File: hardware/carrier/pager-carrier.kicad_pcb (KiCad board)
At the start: 2 copper layers, 38.9 x 48.9 mm, 79 parts, among them J1 PANEL, J2 CARDKB, J3 HAPTIC, J4 EXT_LED, J5 PIEZ, J6 USB4235, J7 BATTERY, J8 FRONTLIGHT, M1 Walter, Q1 UMH3N, Q2 SI1308EDL, Q3 MMST3904, Q4 AO3401A, SW1 KMR221GLFS, SW2 JS102011SAQN, U1 CP2102N-A02-GQFN24, U2 SN74LVC2G126DCUR, U3 DRV2605LDGSR, U4 LIS2DW12TR, U5 BQ25185DLHR, U6 MAX17048G+T10, U7 TPS62840DLCR

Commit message: v0.2 boards release candidate
This has almost everything in both boards but we need
a few part swaps.
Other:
- board text added: "+LED-"
- board text added: "BATT"
- board text added: "CHAM Carrier @awongawong"
- board text added: "FR. L"
- board text added: "HAPTIC"
- board text added: "KBD"
- board text added: "MACH Carrier @awongawong"
- board text added: "PIEZ"
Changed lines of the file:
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@@
 		(layer "Edge.Cuts")
+	)
+	(gr_text "CHAM Carrier\n@awongawong"
+		(at 92.329 105.537 0)
+		(layer "F.SilkS")
+		(effects
+			(font
+				(size 1 1)
+				(thickness 0.1)
+			)
+			(justify left bottom)
+		)
+	)
+	(gr_text "+LED-"
+		(at 81.026 89.662 0)
+		(layer "F.SilkS")
+		(effects
+			(font
+				(size 1 1)
+				(thickness 0.15)
+				(bold yes)
+			)
+			(justify left bottom)
+		)
+	)
+	(gr_text "PIEZ"
+		(at 88.646 89.662 0)
+		(layer "F.SilkS")
+		(effects
+			(font
+				(size 1 1)
+				(thickness 0.15)
+				(bold yes)
+			)
+			(justify left bottom)
+		)
+	)
+	(gr_text "HAPTIC"
+		(at 102.997 97.663 0)
+		(layer "F.SilkS")
+		(effects
+			(font
+				(size 1 1)
+				(thickness 0.15)
+				(bold yes)
+			)
+			(justify left bottom)
+		)
+	)
+	(gr_text "KBD"
+		(at 104.267 105.029 0)
+		(layer "F.SilkS")
+		(effects
+			(font
+				(size 1 1)
+				(thickness 0.15)
+				(bold yes)
+			)
+			(justify left bottom)
+		)
+	)
+	(gr_text "FR. L"
+		(at 104.521 79.121 0)
+		(layer "F.SilkS")
+		(effects
+			(font
+				(size 1 1)
+				(thickness 0.15)
+				(bold yes)
+			)
+			(justify left bottom)
+		)
+	)
+	(gr_text "BATT"
+		(at 106.68 67.056 0)
+		(layer "F.SilkS")
+		(effects
+			(font
+				(size 1 1)
+				(thickness 0.15)
+				(bold yes)
+			)
+			(justify left bottom)
+		)
+	)
+	(gr_text "MACH Carrier\n@awongawong"
+		(at 103.378 105.537 0)
+		(layer "B.SilkS")
+		(effects
+			(font
+				(size 1 1)
+				(thickness 0.1)
+			)
+			(justify left bottom mirror)
+		)
 	)
 	(gr_text "FAB NOTE: trim the 28 Walter header pins flush with the solder fillets after soldering (untrimmed pins reach 5 mm above this board, into the display glass)"

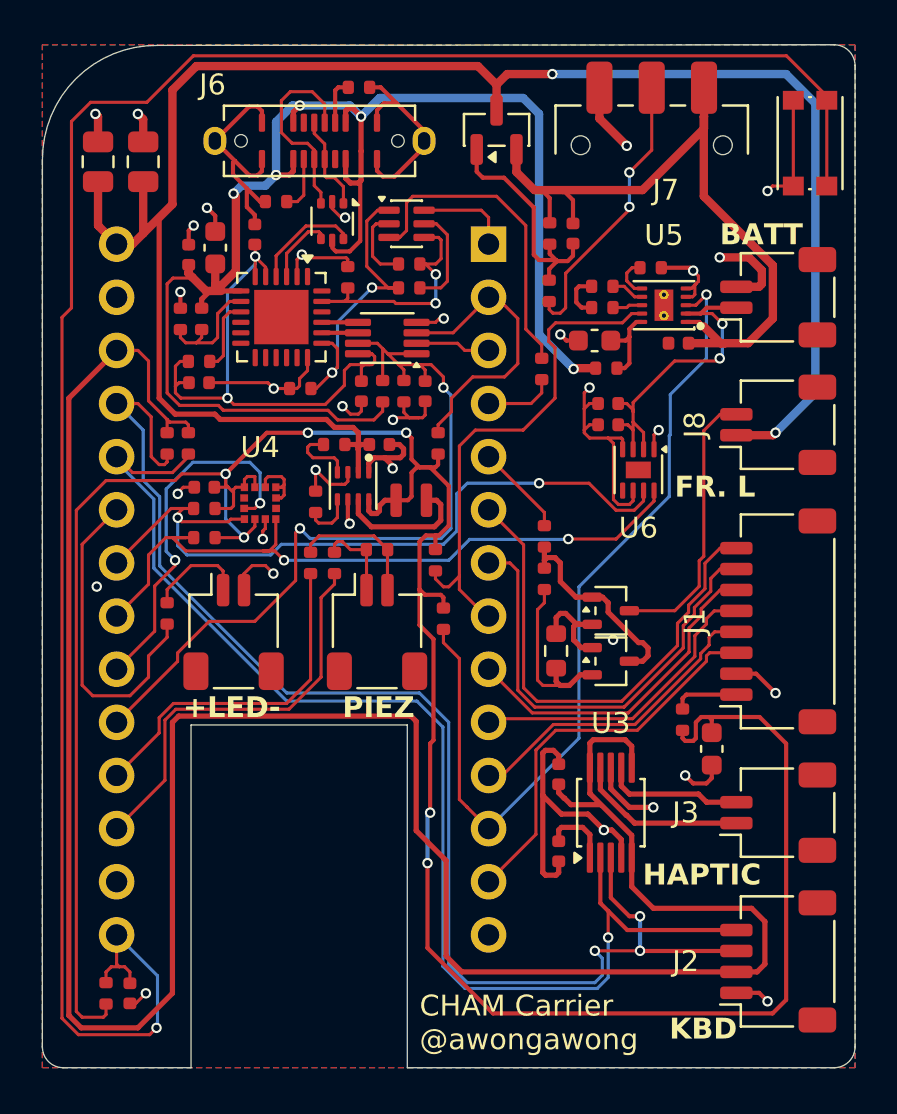
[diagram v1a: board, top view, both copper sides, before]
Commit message: Swap to common parts. v0.2 final.
Panel and carrier should be ready to send to JLPCB now.
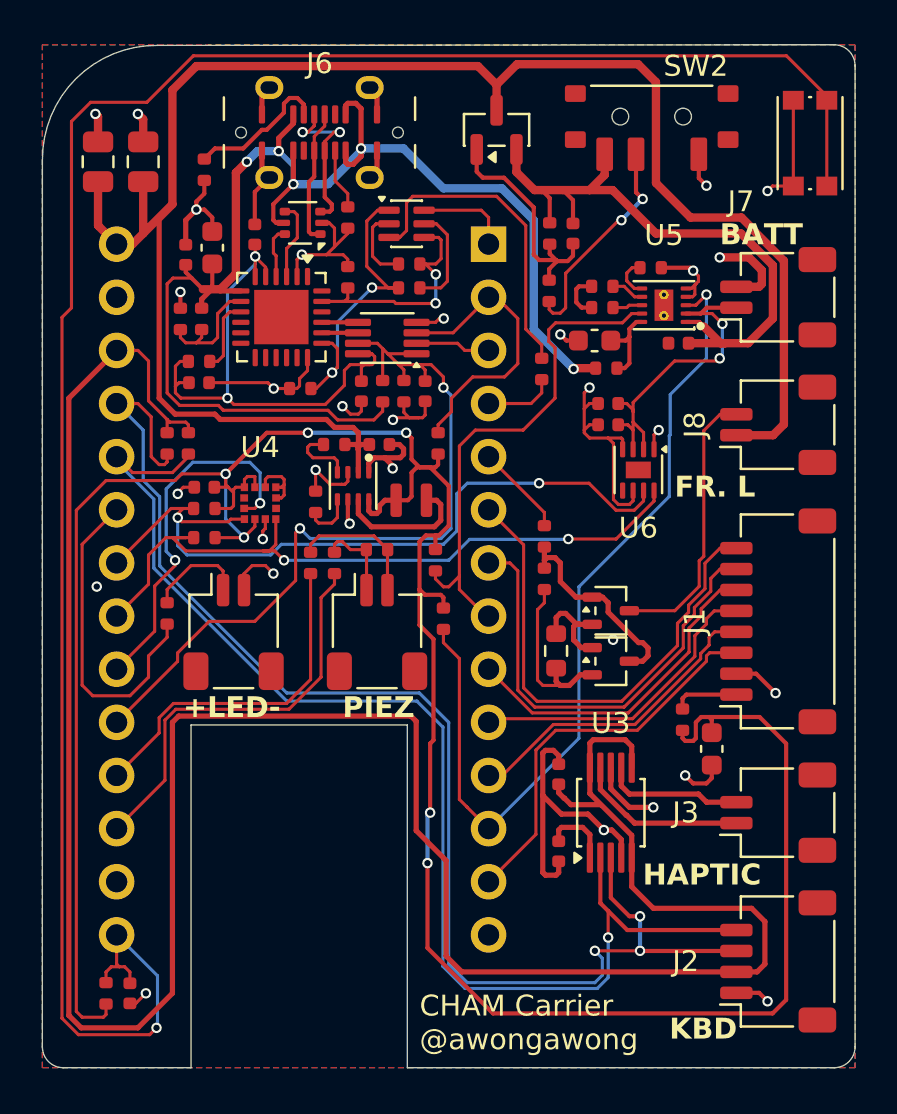
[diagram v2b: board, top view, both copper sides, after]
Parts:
- J6: value USB4235 -> TYPE-C 16PLT-H6.5; footprint pager-carrier:USB_C_Receptacle_GCT_USB4235_Vertical -> pager-carrier:USB_C_Receptacle_ShouHan_TYPE-C-16PLT-H6.5_Vertical
- SW2: value JS102011SAQN -> MSS12C02LS-HB2.0; footprint Button_Switch_SMD:SW_SPDT_CK_JS102011SAQN -> pager-carrier:SW_SPDT_ShouHan_MSS12C02LS_TopActuated
- moved R29 6.25 mm to (88.9, 65.7), turned to -90 degrees
- moved R31 3.75 mm to (82.0, 63.4), turned to -90 degrees
- moved D1 1.41 mm to (86.7, 65.9), turned to 180 degrees
- moved SW2 1.37 mm to (103.4, 60.8), turned to 180 degrees
- moved J6 0.40 mm to (87.5, 61.6)
- moved C1 0.14 mm to (82.4, 67.1)
- moved C2 0.14 mm to (81.2, 67.4)
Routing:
- net GND: track 124.9 -> 113.8 mm, vias 32 -> 30
- net VBUS: track 74.4 -> 67.8 mm
- net /Power/SYS: track 34.7 -> 29.8 mm
- net Net-(J6-CC1): track 2.67 -> 6.82 mm
- net SYS_SW: track 88.9 -> 85.7 mm, vias 2 -> 0
- net Net-(SW2-B): track 13.6 -> 10.4 mm
- net USB_DM: track 5.20 -> 2.50 mm
- net Net-(D1-I/O1-Pad1): track 4.66 -> 6.52 mm
- net Net-(D1-I/O2-Pad3): track 9.51 -> 7.89 mm, vias 0 -> 2
- net Net-(J6-CC2): track 2.23 -> 2.94 mm

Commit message: Finalizing PCB cute designs
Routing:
- net (no net): track 0.00 -> 29.6 mm
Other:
- board text added: "CHAM Carrier @awongawong Oct 2026"
- board text added: "Fr Light"
- board text added: "MACH Carrier @awongawong Oct 2026"
- board text removed: "CHAM Carrier @awongawong"
- board text removed: "FR. L"
- board text removed: "MACH Carrier @awongawong"
